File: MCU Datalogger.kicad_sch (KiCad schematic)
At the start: 0 parts

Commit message: Have added required symbols to the schematic sheets
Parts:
- added BT?: Battery, symbol Device:Battery
- added C?: C_Polarized, symbol Device:C_Polarized
- added C? (x4): C, symbol Device:C
- added D? (x2): LED, symbol Device:LED
- added H? (x4): MountingHole, symbol Mechanical:MountingHole
- added R? (x7): R, symbol Device:R
- added U?: DS1337S+, SOIC127P600X175-8N, symbol DS1337S_:DS1337S+
- added U?: ATMEGA328-AU, QFP80P900X900X120-32N, symbol ATMEGA328-AU:ATMEGA328-AU
- added U? (x2): 24LC1025, symbol Memory_EEPROM:24LC1025
- added Y? (x2): Crystal, symbol Device:Crystal
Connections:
- new net: U?.21 (GND), U?.3 (GND), U?.5 (GND)
- new net: U?.4 (VCC), U?.6 (VCC)
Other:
- added sheet Connectors (Connectors.kicad_sch)

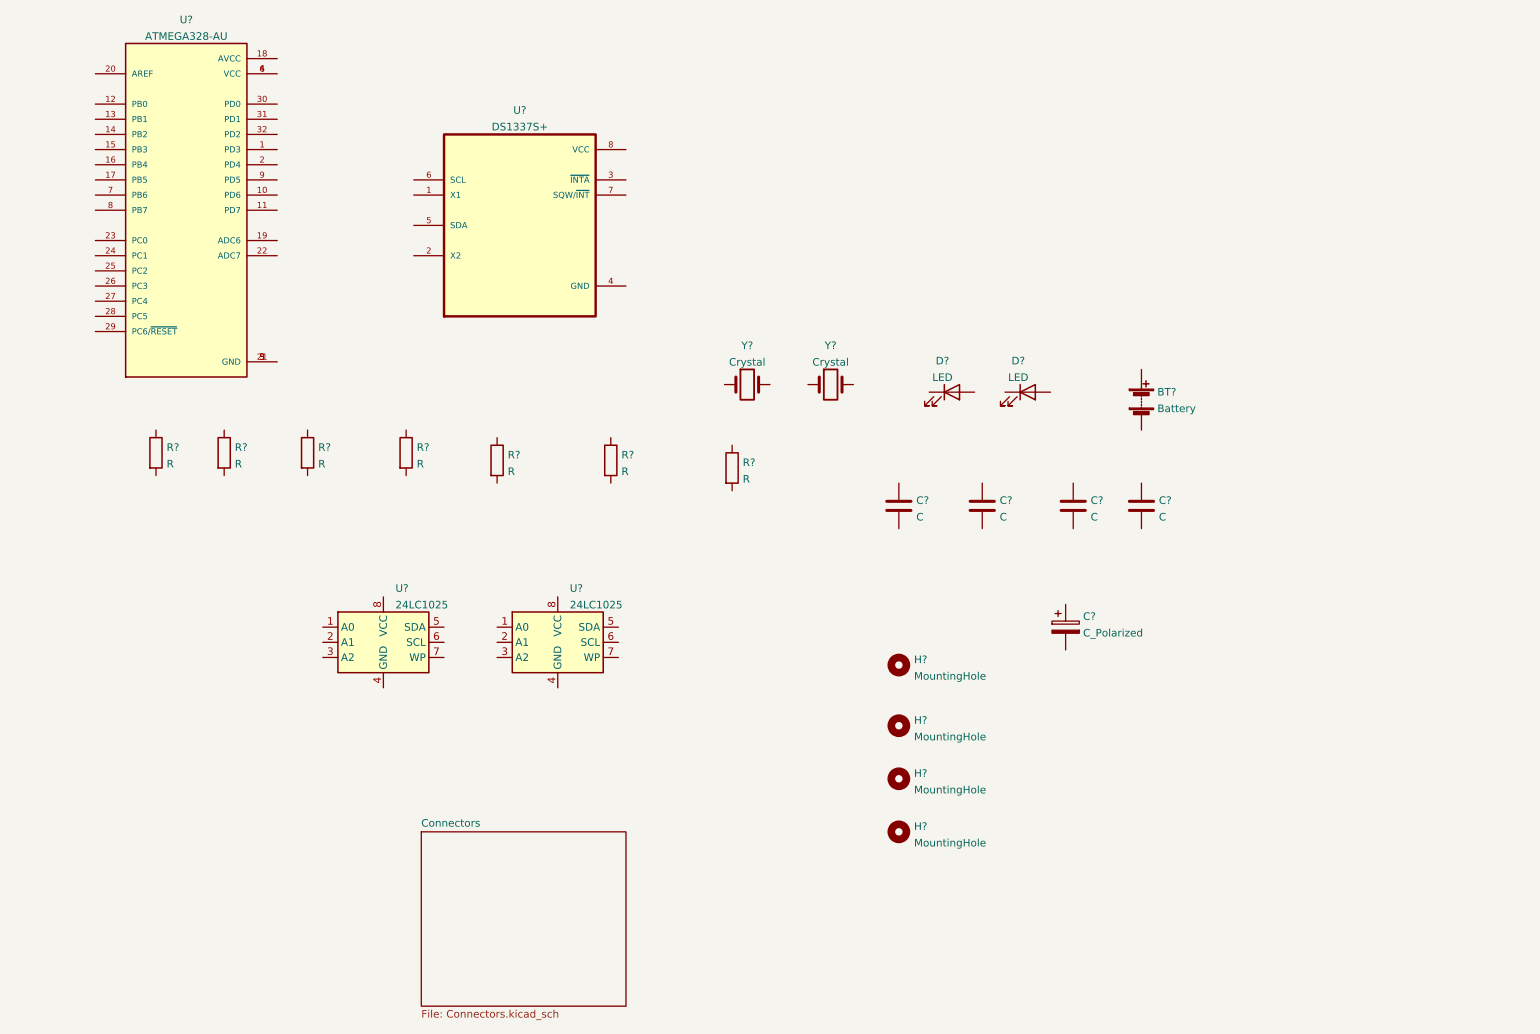
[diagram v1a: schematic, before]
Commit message: Changed locations of symbols
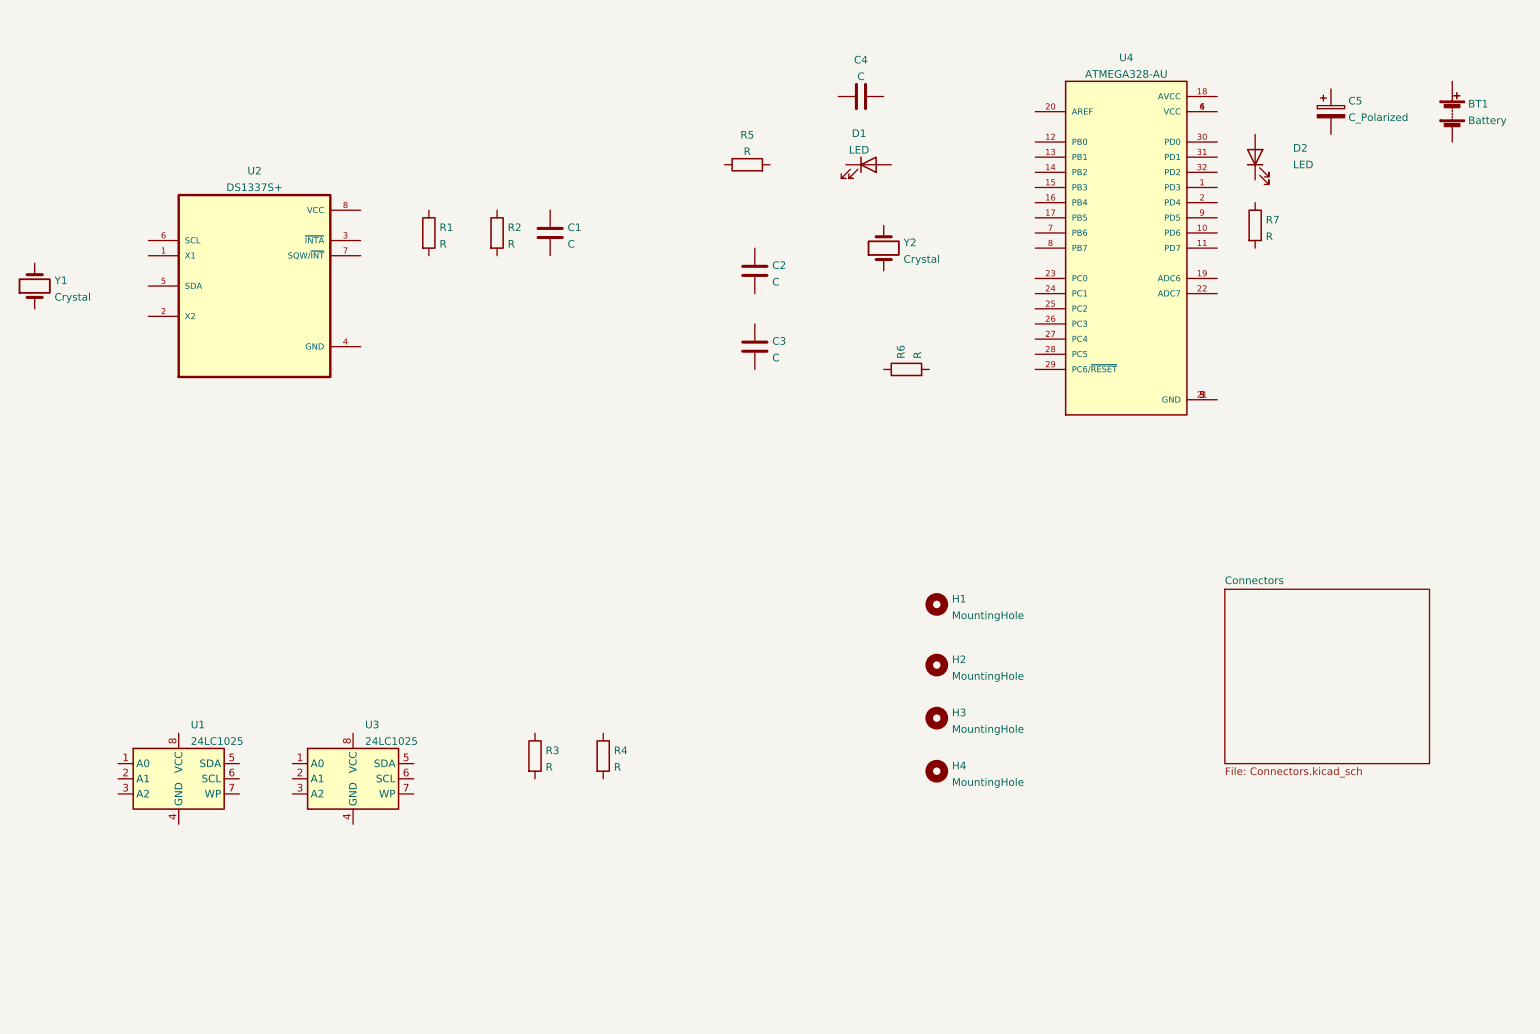
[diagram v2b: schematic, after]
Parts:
- gave numbers to parts that had none: 25
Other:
- moved on the sheet: BT1, C1, C2, C3, C4, C5, D1, D2, H1, H2, H3, H4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

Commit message: Added component values
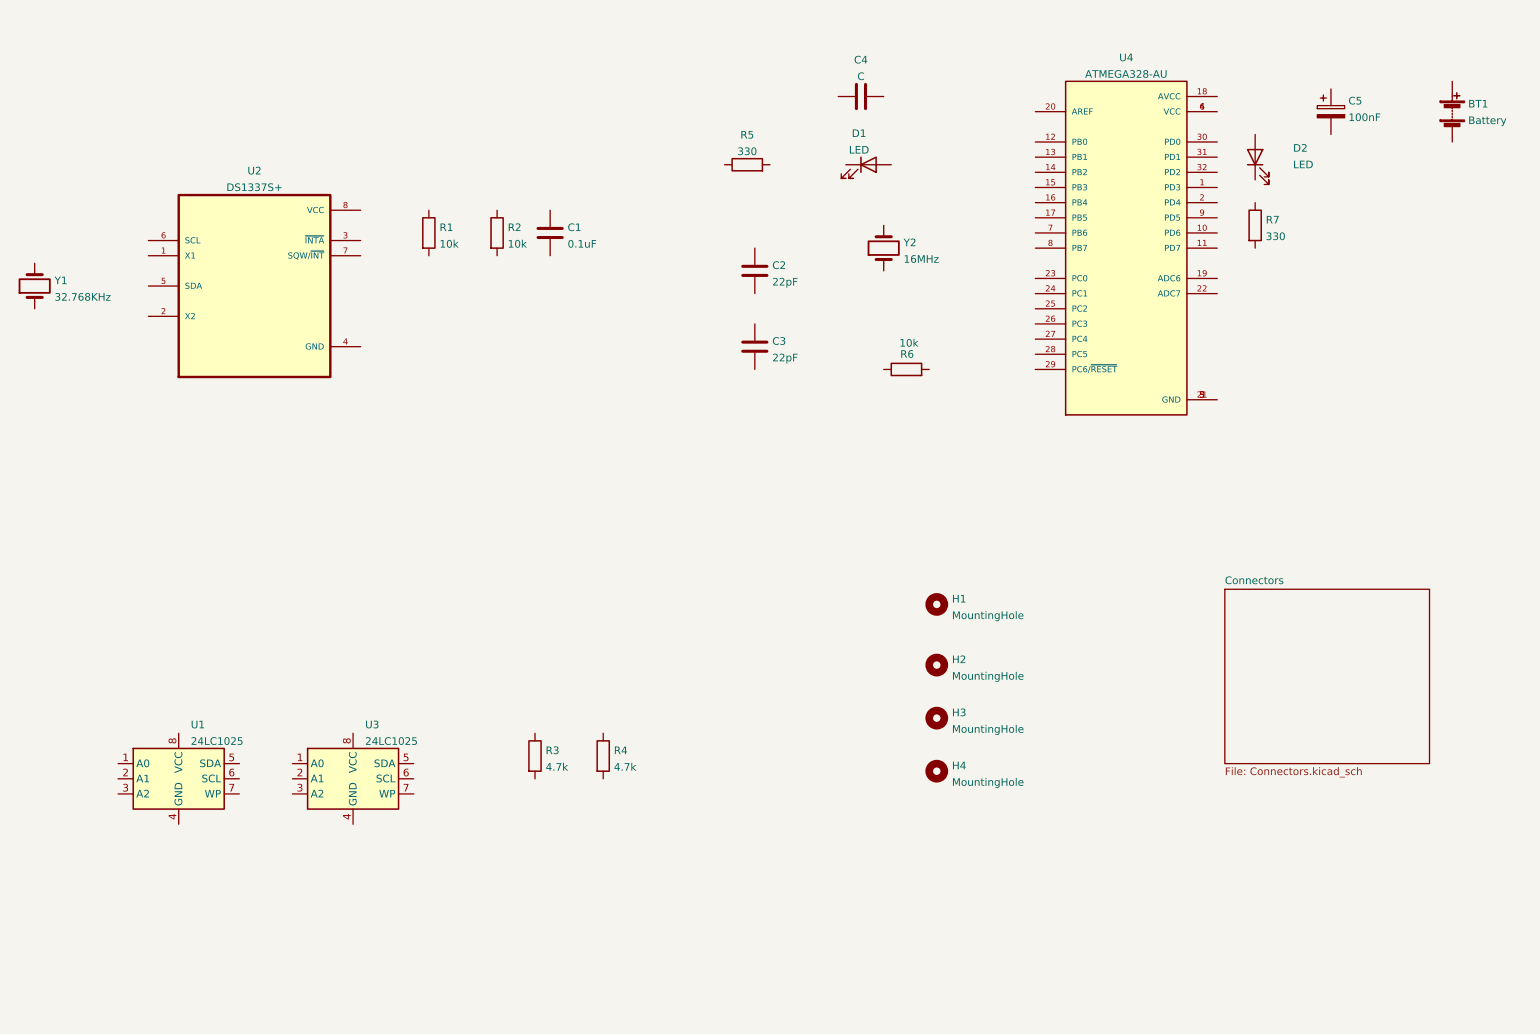
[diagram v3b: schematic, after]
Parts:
- C1: value C -> 0.1uF
- C2, C3: value C -> 22pF
- C5: value C_Polarized -> 100nF
- R1, R2, R6: value R -> 10k
- R3, R4: value R -> 4.7k
- R5, R7: value R -> 330
- Y1: value Crystal -> 32.768KHz
- Y2: value Crystal -> 16MHz
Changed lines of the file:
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@@
       (effects (font (size 1.27 1.27)) (justify left))
     )
-    (property "Value" "C_Polarized" (id 1) (at 249.301 35.2676 0)
+    (property "Value" "100nF" (id 1) (at 249.301 35.2676 0)
       (effects (font (size 1.27 1.27)) (justify left))
     )
@@
       (effects (font (size 1.27 1.27)) (justify left))
     )
-    (property "Value" "R" (id 1) (at 235.458 55.2066 0)
+    (property "Value" "330" (id 1) (at 235.458 55.2066 0)
       (effects (font (size 1.27 1.27)) (justify left))
     )
@@
       (effects (font (size 1.27 1.27)) (justify left))
     )
-    (property "Value" "R" (id 1) (at 126.238 144.1066 0)
+    (property "Value" "4.7k" (id 1) (at 126.238 144.1066 0)
       (effects (font (size 1.27 1.27)) (justify left))
     )
@@
       (effects (font (size 1.27 1.27)) (justify left))
     )
-    (property "Value" "C" (id 1) (at 152.781 62.8266 0)
+    (property "Value" "22pF" (id 1) (at 152.781 62.8266 0)
       (effects (font (size 1.27 1.27)) (justify left))
     )
@@
       (effects (font (size 1.27 1.27)) (justify left))
     )
-    (property "Value" "R" (id 1) (at 97.028 56.4766 0)
+    (property "Value" "10k" (id 1) (at 97.028 56.4766 0)
       (effects (font (size 1.27 1.27)) (justify left))
     )
@@
       (effects (font (size 1.27 1.27)) (justify left))
     )
-    (property "Value" "R" (id 1) (at 114.808 144.1066 0)
+    (property "Value" "4.7k" (id 1) (at 114.808 144.1066 0)
       (effects (font (size 1.27 1.27)) (justify left))
     )
@@
       (effects (font (size 1.27 1.27)) (justify left))
     )
-    (property "Value" "C" (id 1) (at 118.491 56.4766 0)
+    (property "Value" "0.1uF" (id 1) (at 118.491 56.4766 0)
       (effects (font (size 1.27 1.27)) (justify left))
     )
@@
   (symbol (lib_id "Device:R") (at 175.26 77.47 90) (unit 1)
     (in_bom yes) (on_board yes)
-    (property "Reference" "R6" (id 0) (at 174.3515 75.692 0)
-      (effects (font (size 1.27 1.27)) (justify left))
-    )
-    (property "Value" "R" (id 1) (at 177.1266 75.692 0)
+    (property "Reference" "R6" (id 0) (at 176.53 74.93 90)
+      (effects (font (size 1.27 1.27)) (justify left))
+    )
+    (property "Value" "10k" (id 1) (at 177.292 73.0634 90)
       (effects (font (size 1.27 1.27)) (justify left))
     )
@@
       (effects (font (size 1.27 1.27)) (justify right))
     )
-    (property "Value" "Crystal" (id 1) (at 174.7774 59.0166 90)
+    (property "Value" "16MHz" (id 1) (at 174.7774 59.0166 90)
       (effects (font (size 1.27 1.27)) (justify right))
     )
@@
       (effects (font (size 1.27 1.27)) (justify right))
     )
-    (property "Value" "Crystal" (id 1) (at 32.5374 65.3666 90)
+    (property "Value" "32.768KHz" (id 1) (at 32.5374 65.3666 90)
       (effects (font (size 1.27 1.27)) (justify right))
     )
@@
       (effects (font (size 1.27 1.27)) (justify left))
     )
-    (property "Value" "C" (id 1) (at 152.781 75.5266 0)
+    (property "Value" "22pF" (id 1) (at 152.781 75.5266 0)
       (effects (font (size 1.27 1.27)) (justify left))
     )
@@
       (effects (font (size 1.27 1.27)) (justify left))
     )
-    (property "Value" "R" (id 1) (at 108.458 56.4766 0)
+    (property "Value" "10k" (id 1) (at 108.458 56.4766 0)
       (effects (font (size 1.27 1.27)) (justify left))
     )
@@
     (in_bom yes) (on_board yes) (fields_autoplaced)
     (property "Reference" "R5" (id 0) (at 148.59 38.1975 90))
-    (property "Value" "R" (id 1) (at 148.59 40.9726 90))
+    (property "Value" "330" (id 1) (at 148.59 40.9726 90))
     (property "Footprint" "" (id 2) (at 148.59 44.958 90)
       (effects (font (size 1.27 1.27)) hide)
@@
     )
     (path "/76acfa45-f969-4555-894c-92213c0bf6ef"
-      (reference "C1") (unit 1) (value "C") (footprint "")
+      (reference "C1") (unit 1) (value "0.1uF") (footprint "")
     )
     (path "/289b5e4e-f501-42cb-a9be-667823e7e039"
-      (reference "C2") (unit 1) (value "C") (footprint "")
+      (reference "C2") (unit 1) (value "22pF") (footprint "")
     )
     (path "/b56a12ea-b784-418f-9fd1-6ae3e4fa7f0f"
-      (reference "C3") (unit 1) (value "C") (footprint "")
+      (reference "C3") (unit 1) (value "22pF") (footprint "")
     )
     (path "/13ed7e99-5fcc-4813-8dc4-658e15de375f"
@@
     )
     (path "/0f8e409e-cf6d-4563-bb15-9cdba03d63e0"
-      (reference "C5") (unit 1) (value "C_Polarized") (footprint "")
+      (reference "C5") (unit 1) (value "100nF") (footprint "")
     )
     (path "/7e11d82d-5f1a-4621-8ade-7613d1578ae6"
@@
     )
     (path "/36b6e7f7-2dca-423a-bcef-fde9aa2801b3"
-      (reference "R1") (unit 1) (value "R") (footprint "")
+      (reference "R1") (unit 1) (value "10k") (footprint "")
     )
     (path "/d47860b8-b6b7-467e-ae49-e649184ee0dd"
-      (reference "R2") (unit 1) (value "R") (footprint "")
+      (reference "R2") (unit 1) (value "10k") (footprint "")
     )
     (path "/4bcd427c-6da5-4a16-9e22-644cbce14409"
-      (reference "R3") (unit 1) (value "R") (footprint "")
+      (reference "R3") (unit 1) (value "4.7k") (footprint "")
     )
     (path "/25be5f5f-50ef-4d4b-9ddb-de95537a9f8e"
-      (reference "R4") (unit 1) (value "R") (footprint "")
+      (reference "R4") (unit 1) (value "4.7k") (footprint "")
     )
     (path "/f4f88d11-cd1c-4f93-88f6-5a2a85c4fb95"
-      (reference "R5") (unit 1) (value "R") (footprint "")
+      (reference "R5") (unit 1) (value "330") (footprint "")
     )
     (path "/92717230-1552-4341-b118-927c004a8d6d"
-      (reference "R6") (unit 1) (value "R") (footprint "")
+      (reference "R6") (unit 1) (value "10k") (footprint "")
     )
     (path "/17f36fd0-1613-495a-8fa5-7233612eb09e"
-      (reference "R7") (unit 1) (value "R") (footprint "")
+      (reference "R7") (unit 1) (value "330") (footprint "")
     )
     (path "/d08e6379-4558-405f-b81c-98df4fde98c8"
@@
     )
     (path "/a107f895-390a-45c8-b926-bb94c406e415"
-      (reference "Y1") (unit 1) (value "Crystal") (footprint "")
+      (reference "Y1") (unit 1) (value "32.768KHz") (footprint "")
     )
     (path "/9b495040-abbc-4ab3-9727-8b17dc235939"
-      (reference "Y2") (unit 1) (value "Crystal") (footprint "")
-    )
-  )
+      (reference "Y2") (unit 1) (value "16MHz") (footprint "")
+    )
+  )

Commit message: Completed symbol-footprint associations
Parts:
- BT1: footprint (none) -> Connector_PinHeader_2.54mm:PinHeader_1x02_P2.54mm_Horizontal
- C1, C2, C3, C4, C5: footprint (none) -> Capacitor_SMD:C_0805_2012Metric
- D1, D2: footprint (none) -> LED_SMD:LED_0805_2012Metric
- H1, H2, H3, H4: footprint (none) -> MountingHole:MountingHole_2.1mm
- R1, R2, R3, R4, R5, R6, R7: footprint (none) -> Resistor_SMD:R_0805_2012Metric
- U1, U3: footprint (none) -> Package_SO:SOIC-8_5.23x5.23mm_P1.27mm
- Y1, Y2: footprint (none) -> Crystal:Crystal_SMD_5032-2Pin_5.0x3.2mm_HandSoldering

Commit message: Wiring
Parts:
- C4: value C -> 0.1uF
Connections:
- net at C5.1: now also BT1.1 (+), D2.2 (A), U4.18 (AVCC), U4.4 (VCC)
- net GND: now reaches C5.2
- net GND: now also BT1.2 (-), C1.2, C2.1, C3.1, C4.1, R5.1, R7.2, U1.4 (GND), U1.7 (WP), U2.4 (GND), U3.4 (GND), U3.7 (WP), U4.21 (GND), U4.3 (GND), U4.5 (GND)
- net at C4.2: now also U4.20 (AREF)
- net at R7.1: now also D2.1 (K)
- net at U2.1 (X1): now also Y1.2
- net at U2.2 (X2): now also Y1.1
- net at U2.3 (~{INTA}): now also R1.2
- net SDA: now reaches U2.5 (SDA)
- net SDA: now also R4.2, U1.5 (SDA), U3.5 (SDA), U4.27 (PC4)
- net SCK: now reaches U2.6 (SCL)
- net SCK: now also D1.2 (A), R3.2, U1.6 (SCL), U3.6 (SCL), U4.17 (PB5), U4.28 (PC5)
- net at U2.7 (SQW/~{INT}): now also R2.2
- net Vcc: now reaches U2.8 (VCC)
- net Vcc: now also C1.1, R1.1, R2.1, R6.1, U1.1 (A0), U1.2 (A1), U1.3 (A2), U1.8 (VCC), U3.1 (A0), U3.2 (A1), U3.3 (A2), U3.8 (VCC)
- net at R4.1: now also R3.1
- net D3: now reaches U4.1 (PD3)
- net D6: now reaches U4.10 (PD6)
- net D7: now reaches U4.11 (PD7)
- net D8: now reaches U4.12 (PB0)
- net MOSI: now reaches U4.15 (PB3)
- net MISO: now reaches U4.16 (PB4)
- net D4: now reaches U4.2 (PD4)
- net RESET: now reaches U4.29 (PC6/~{RESET})
- net RESET: now also R6.2
- net RX: now reaches U4.30 (PD0)
- net Tx: now reaches U4.31 (PD1)
- net D2: now reaches U4.32 (PD2)
- net at U4.6 (VCC): no longer U4.4 (VCC)
- net at U4.7 (PB6): now also C2.2, Y2.2
- net at U4.8 (PB7): now also C3.2, Y2.1
- net D5: now reaches U4.9 (PD5)
- net at D1.1 (K): now also R5.2
- no-connect marks 0 -> 9
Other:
- moved on the sheet: BT1, C2, C3, C4, C5, D1, D2, R5, R7, Y2

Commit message: final Wiring
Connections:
- net Tx renamed TX
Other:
- sheet Connectors ports: added D2, D3, D4, D5, D6, D7, D8, GND, MISO, MOSI, RESET, RX, SCK, SDA, TX, Vcc; removed none
